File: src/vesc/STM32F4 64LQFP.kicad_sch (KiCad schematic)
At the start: 16 parts, among them J7 Conn_02x03_Odd_Even, U5 STM32F405RGT6, X1 24MHz

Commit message: footprints - connectors, mounting holes, inductor
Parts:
- J7: footprint (none) -> Connector_PinHeader_1.27mm:PinHeader_2x03_P1.27mm_Vertical_SMD
- X1: footprint (none) -> Crystal:Crystal_SMD_2016-4Pin_2.0x1.6mm
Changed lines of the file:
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@@
 			)
 		)
-		(property "Footprint" ""
+		(property "Footprint" "Crystal:Crystal_SMD_2016-4Pin_2.0x1.6mm"
 			(at 207.01 52.07 0)
 			(effects
@@
 			)
 		)
-		(property "Footprint" ""
+		(property "Footprint" "Connector_PinHeader_1.27mm:PinHeader_2x03_P1.27mm_Vertical_SMD"
 			(at 248.92 78.74 0)
 			(effects

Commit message: Correct footprints
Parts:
- U5: footprint CRF1:lqfp64_pad_mod -> Package_QFP:LQFP-64_10x10mm_P0.5mm
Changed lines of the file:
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@@
 			)
 		)
-		(property "Footprint" "CRF1:lqfp64_pad_mod"
+		(property "Footprint" "Package_QFP:LQFP-64_10x10mm_P0.5mm"
 			(at 146.05 99.06 0)
 			(effects

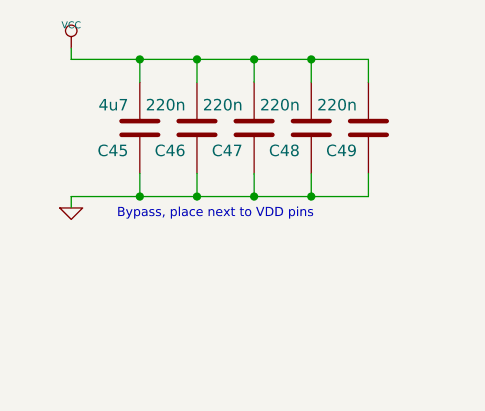
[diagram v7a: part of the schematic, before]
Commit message: component placement
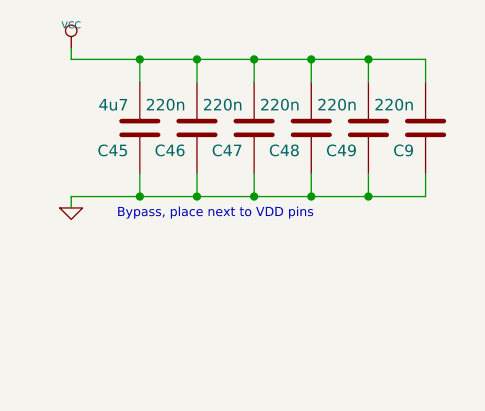
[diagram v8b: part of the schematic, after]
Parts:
- added C9: 220n, Capacitor_SMD:C_0402_1005Metric, symbol BLDC_4-rescue:C-RESCUE-BLDC_4
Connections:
- net GND: now also C9.1
- net VCC: now also C9.2
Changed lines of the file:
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@@
 	)
 	(junction
+		(at 264.16 40.64)
+		(diameter 0)
+		(color 0 0 0 0)
+	)
+	(junction
 		(at 245.11 40.64)
 		(diameter 0)
@@
 	)
 	(junction
+		(at 264.16 25.4)
+		(diameter 0)
+		(color 0 0 0 0)
+	)
+	(junction
 		(at 238.76 40.64)
 		(diameter 0)
@@
 	(wire
 		(pts
+			(xy 270.51 25.4) (xy 270.51 27.94)
+		)
+		(stroke
+			(width 0)
+			(type default)
+		)
+	)
+	(wire
+		(pts
 			(xy 231.14 25.4) (xy 238.76 25.4)
 		)
@@
 	(wire
 		(pts
+			(xy 270.51 40.64) (xy 270.51 38.1)
+		)
+		(stroke
+			(width 0)
+			(type default)
+		)
+	)
+	(wire
+		(pts
 			(xy 184.15 154.94) (xy 185.42 154.94)
 		)
@@
 	(wire
 		(pts
+			(xy 264.16 40.64) (xy 270.51 40.64)
+		)
+		(stroke
+			(width 0)
+			(type default)
+		)
+	)
+	(wire
+		(pts
 			(xy 181.61 153.67) (xy 181.61 161.29)
 		)
@@
 	(wire
 		(pts
+			(xy 264.16 25.4) (xy 270.51 25.4)
+		)
+		(stroke
+			(width 0)
+			(type default)
+		)
+	)
+	(wire
+		(pts
 			(xy 196.85 39.37) (xy 215.9 39.37)
 		)
@@
 					(unit 1)
 				)
+			)
+		)
+	)
+	(symbol
+		(lib_id "BLDC_4-rescue:C-RESCUE-BLDC_4")
+		(at 270.51 33.02 180)
+		(unit 1)
+		(exclude_from_sim no)
+		(in_bom yes)
+		(on_board yes)
+		(dnp no)
+		(property "Reference" "C9"
+			(at 269.24 35.56 0)
+			(effects
+				(font
+					(size 1.27 1.27)
+				)
+				(justify left)
+			)
+		)
+		(property "Value" "220n"
+			(at 269.24 30.48 0)
+			(effects
+				(font
+					(size 1.27 1.27)
+				)
+				(justify left)
+			)
+		)
+		(property "Footprint" "Capacitor_SMD:C_0402_1005Metric"
+			(at 270.51 33.02 0)
+			(effects
+				(font
+					(size 1.524 1.524)
+				)
+				(hide yes)
+			)
+		)
+		(property "Datasheet" ""
+			(at 270.51 33.02 0)
+			(effects
+				(font
+					(size 1.524 1.524)
+				)
+				(hide yes)
+			)
+		)
+		(property "Description" ""
+			(at 270.51 33.02 0)
+			(effects
+				(font
+					(size 1.27 1.27)
+				)
+			)
+		)
+		(pin "1"
+		)
+		(pin "2"
+		)
+		(instances
+			(project "Cheap FOCer 2 60mm"
+				(path "/8b53313b-c20e-4d2c-aeda-56c30dbca1c0/00000000-0000-0000-0000-000053f7501a"
+					(reference "C9")
+					(unit 1)
+				)
